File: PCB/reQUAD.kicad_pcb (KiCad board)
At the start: 2 copper layers, 51.3 x 18.3 mm, 12 parts, among them J1 Model_100_System_BUS, U1 AS6C1008, U2 74x573, U3 74x2G79, U4 74x02

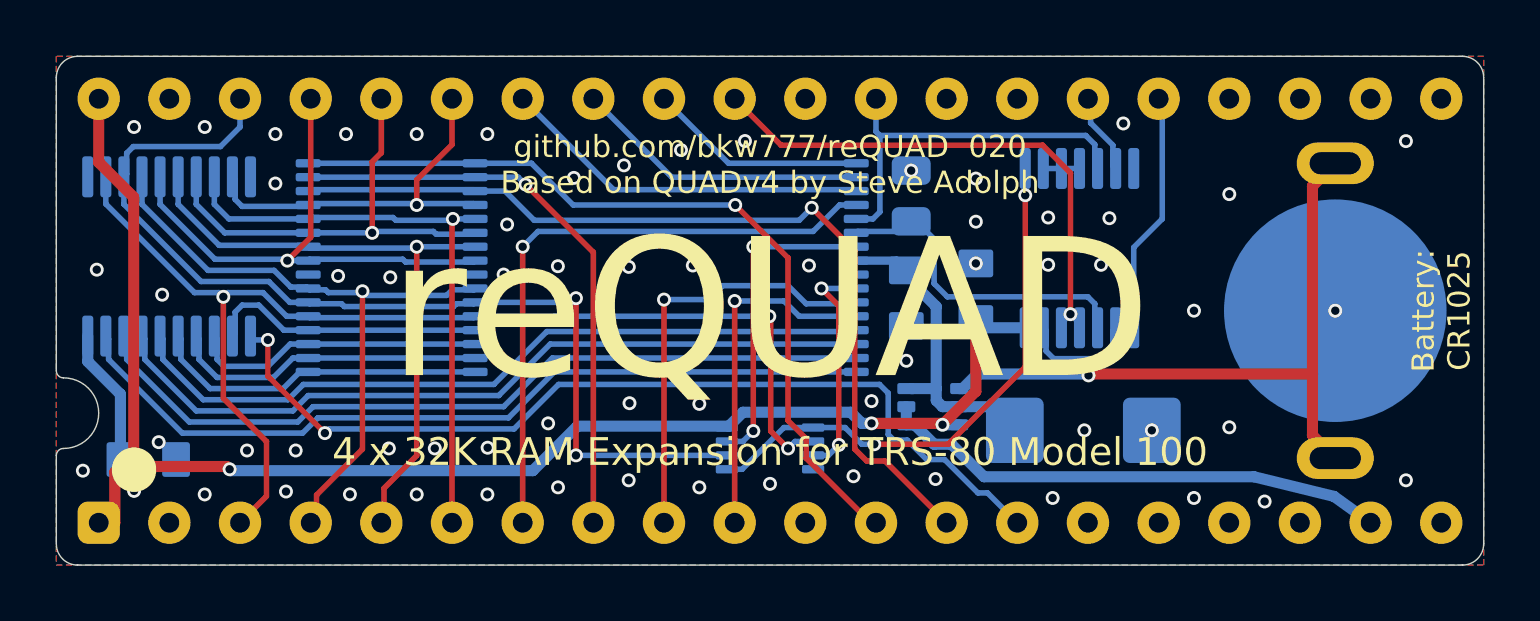
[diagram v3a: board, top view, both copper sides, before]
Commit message: add series resistor on tantalum
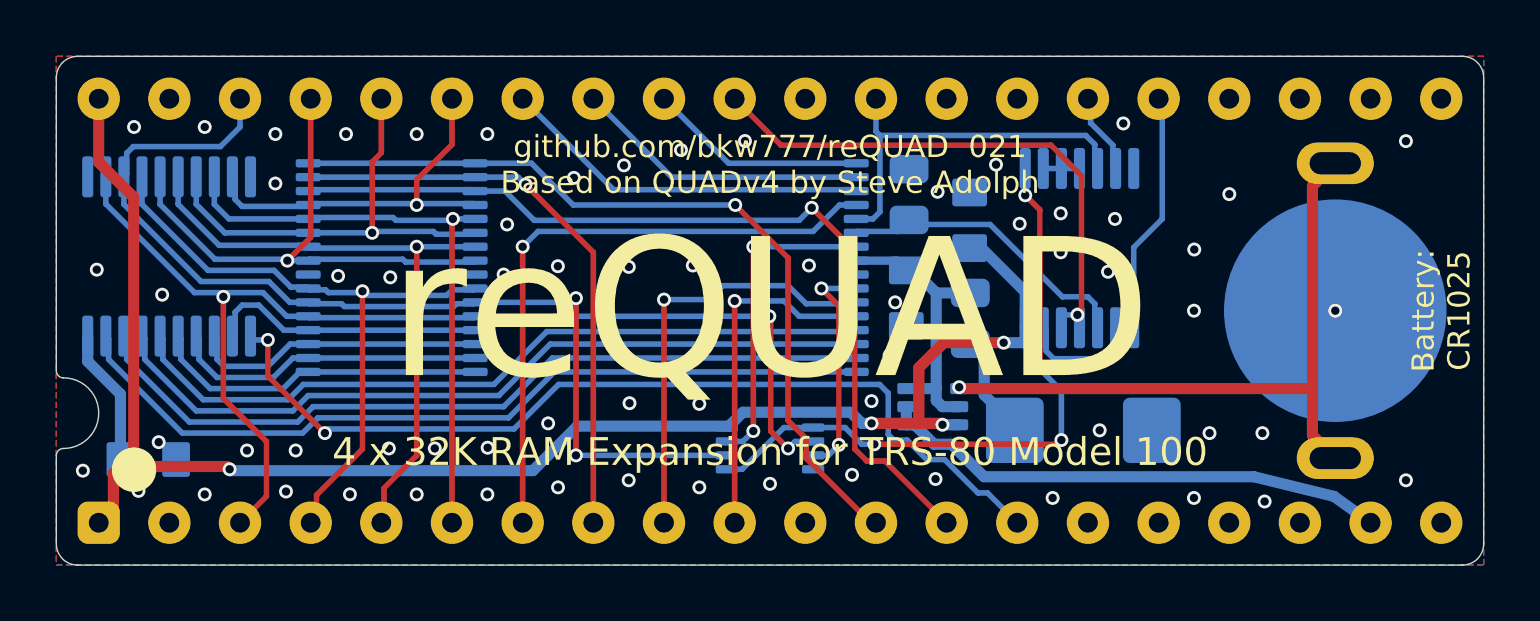
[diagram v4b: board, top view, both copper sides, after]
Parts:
- added R2: 1k, 000_LOCAL:R_0805, B.Cu at (157.2, 100.3)
- moved C3 2.56 mm to (157.2, 96.8)
- moved R1 0.09 mm to (155.0, 95.8)
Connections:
- C4 pad 1: VMEM -> Net-(C4-Pad1)
- U1 pad 9: GND -> unconnected-(U1-NC-Pad9)
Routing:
- net VBUS: track 58.7 -> 63.1 mm
- net Net-(C4-Pad1): track 0.00 -> 4.07 mm
- net /BANK_LATCH: track 19.9 -> 23.3 mm, vias 2 -> 4
- net VMEM: track 11.2 -> 10.3 mm
- net /RAM_CE2: track 11.8 -> 10.9 mm
- net /BUS_A15: track 19.5 -> 20.2 mm
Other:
- board text added: "C1:${00000000-0000-0000-0000-00006082f7c9:VALUE} C3:${f7501592-b6e5-41cf-84c0-263deadb2362:VALUE}"
- board text added: "R1:${2e007350-c3e0-4b02-ad80-1f48bc9a9a17:VALUE} R2:${c9ddfe98-400f-4ef9-b959-878c201bac72:VALUE}"

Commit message: routing R2
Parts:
- moved C4 0.08 mm to (161.3, 104.4)
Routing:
- net /BANK_LATCH: track 23.3 -> 20.8 mm, vias 4 -> 2
- net VBUS: track 63.1 -> 63.7 mm
- net Net-(C4-Pad1): track 4.07 -> 3.78 mm, vias 0 -> 2

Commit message: R1 more common value
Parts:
- R1: value 500k -> 470k
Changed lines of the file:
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@@
     (fp_arc (start 4.905239 -2.551328) (mid 4.8 -2.952056) (end 4.906989 -3.352321)
       (stroke (width 0.1) (type default)) (layer "B.SilkS"))
-    (fp_arc (start 5.224755 -1.996844) (mid 5.280913 -1.852059) (end 5.3 -1.697943)
+    (fp_arc (start 5.224755 -1.996844) (mid 5.280899 -1.852058) (end 5.3 -1.697943)
       (stroke (width 0.1) (type default)) (layer "B.SilkS"))
     (fp_line (start -6.35 -1.6375) (end -6.35 1.6375)
@@
         (effects (font (size 0.8 0.8) (thickness 0.1)) (justify right mirror))
     )
-    (fp_text value "500k" (at -2 -0.075 unlocked) (layer "B.Fab")
+    (fp_text value "470k" (at -2 -0.075 unlocked) (layer "B.Fab")
         (effects (font (size 0.8 0.8) (thickness 0.1)) (justify mirror))
     )

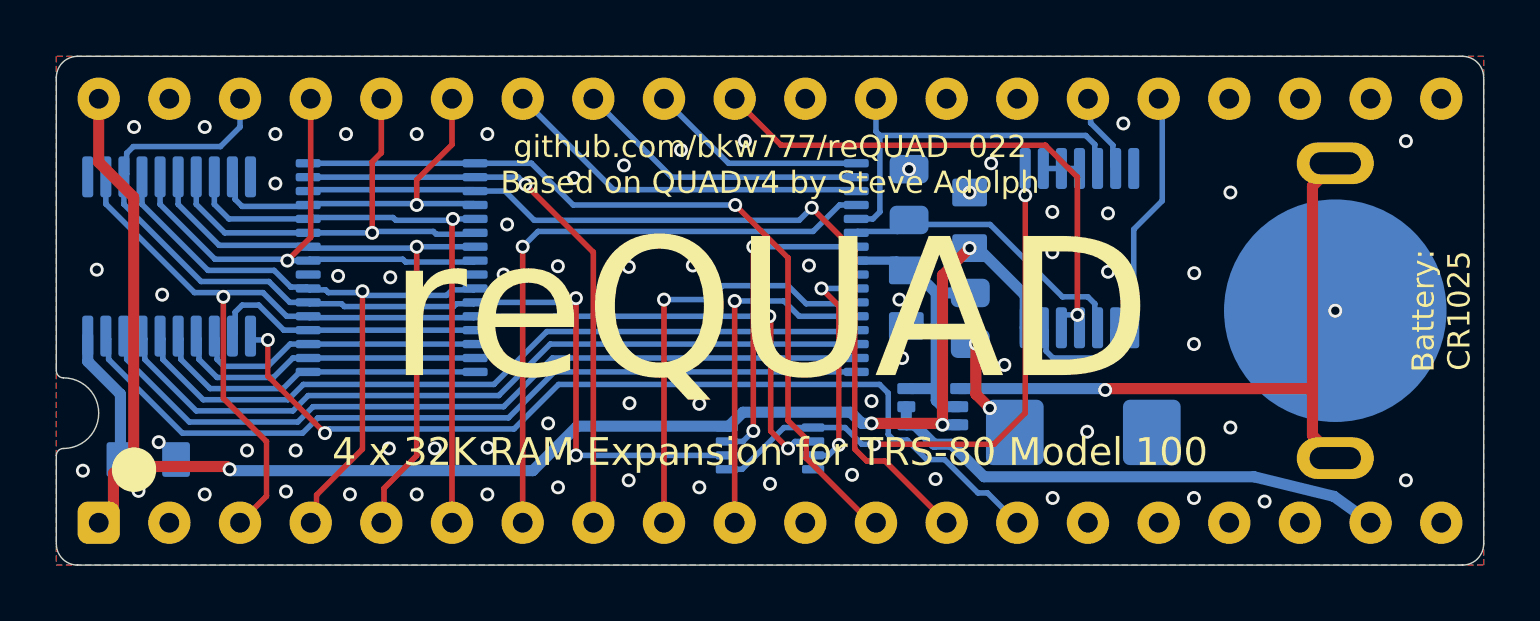
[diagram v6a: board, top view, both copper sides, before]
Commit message: add fiducials
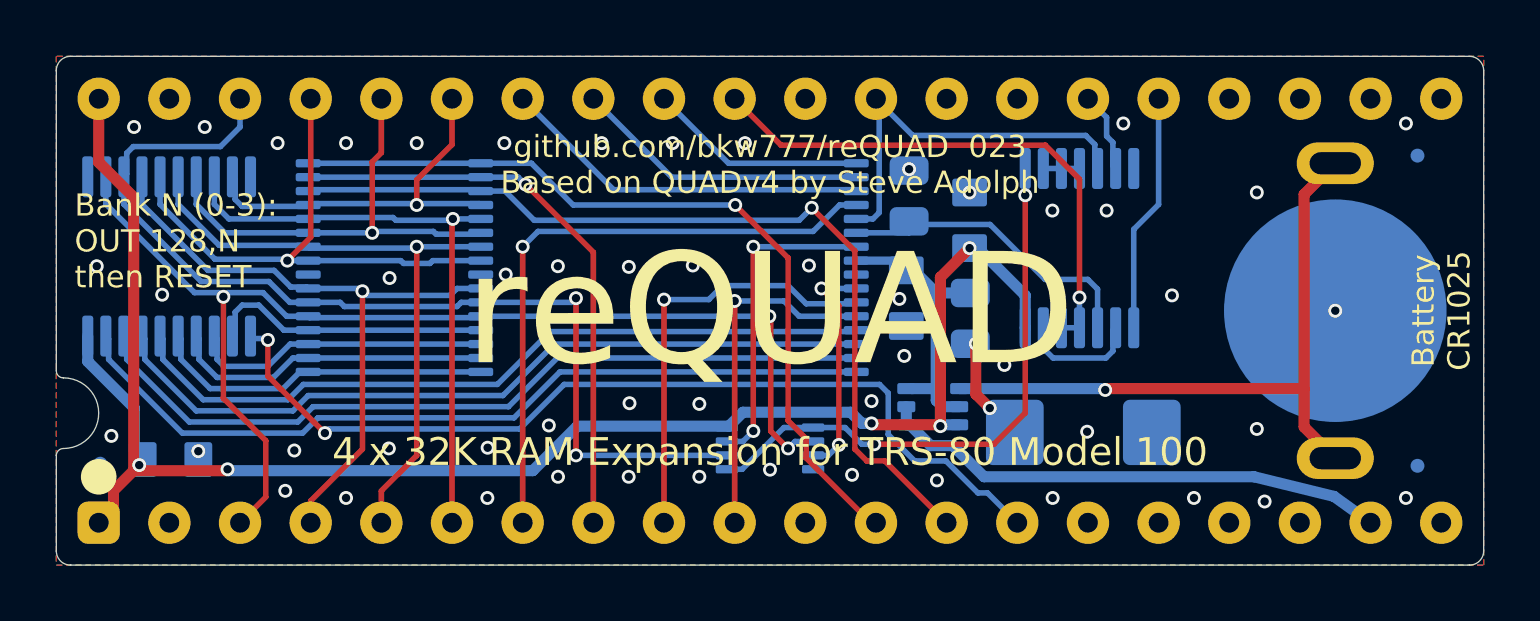
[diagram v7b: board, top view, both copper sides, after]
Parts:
- added F1: Fiducial_0.5_1.0, 000_LOCAL:Fiducial_0.5_1.0, B.Cu at (125.9, 105.5)
- added F2: Fiducial_0.5_1.0, 000_LOCAL:Fiducial_0.5_1.0, B.Cu at (173.3, 105.6)
- added F3: Fiducial_0.5_1.0, 000_LOCAL:Fiducial_0.5_1.0, B.Cu at (173.3, 94.4)
- J1: footprint 000_LOCAL:DIP-40_pins -> 000_LOCAL:DIP-40_PCB
- moved C1 0.80 mm to (128.4, 105.3)
- renumbered C2 to C1, C1 to C2, R2 to R1, R1 to R2
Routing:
- net VMEM: track 10.3 -> 9.59 mm
- net /~{WR}: track 13.8 -> 14.5 mm
- net /RAM_CE2: track 10.9 -> 11.5 mm
- net GND: vias 66 -> 53
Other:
- outline, holes or cut-outs redrawn
- board text added: "${TITLE}"
- board text added: "Bank N (0-3): OUT 128,N then RESET"
- board text added: "Battery CR1025"
- board text added: "C2:${00000000-0000-0000-0000-00006082f7c9:VALUE} C3:${f7501592-b6e5-41cf-84c0-263deadb2362:VALUE}"
- board text added: "R1:${c9ddfe98-400f-4ef9-b959-878c201bac72:VALUE} R2:${2e007350-c3e0-4b02-ad80-1f48bc9a9a17:VALUE}"
- board text removed: "Battery: CR1025"
- board text removed: "C1:${00000000-0000-0000-0000-00006082f7c9:VALUE} C3:${f7501592-b6e5-41cf-84c0-263deadb2362:VALUE}"
- board text removed: "R1:${2e007350-c3e0-4b02-ad80-1f48bc9a9a17:VALUE} R2:${c9ddfe98-400f-4ef9-b959-878c201bac72:VALUE}"
- board text removed: "reQUAD"

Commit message: silkscreen
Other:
- board text added: "Select Bank # (0-3) OUT 128,# Then press RESET"
- board text added: "github.com/bkw777/reQUAD ${REVISION} Based on QUAD by Steve Adolph"
- board text removed: "Bank N (0-3): OUT 128,N then RESET"
- board text removed: "github.com/bkw777/reQUAD ${REVISION} Based on QUADv4 by Steve Adolph"
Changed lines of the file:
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@@
     (fp_arc (start 4.905239 -2.551328) (mid 4.8 -2.952056) (end 4.906989 -3.352321)
       (stroke (width 0.12) (type default)) (layer "B.SilkS"))
-    (fp_arc (start 5.224755 -1.996844) (mid 5.280901 -1.852056) (end 5.3 -1.697943)
+    (fp_arc (start 5.224755 -1.996844) (mid 5.280886 -1.852055) (end 5.3 -1.697943)
       (stroke (width 0.12) (type default)) (layer "B.SilkS"))
     (fp_line (start -6.35 -1.6375) (end -6.35 1.6375)
@@
     (effects (font (size 0.8 0.8) (thickness 0.1)))
   )
-  (gr_text "github.com/bkw777/reQUAD  ${REVISION}\nBased on QUADv4 by Steve Adolph" (at 150 94.75) (layer "F.SilkS")
+  (gr_text "github.com/bkw777/reQUAD  ${REVISION}\nBased on QUAD by Steve Adolph" (at 150 94.75) (layer "F.SilkS")
     (effects (font (size 0.8 0.8) (thickness 0.1)))
   )
-  (gr_text "Bank N (0-3):\nOUT 128,N\nthen RESET" (at 125 97.5) (layer "F.SilkS")
+  (gr_text "Select Bank # (0-3)\nOUT 128,#\nThen press RESET\n" (at 125.235 95.809) (layer "F.SilkS")
     (effects (font (size 0.8 0.8) (thickness 0.1)) (justify left))
   )
